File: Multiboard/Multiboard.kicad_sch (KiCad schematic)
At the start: 0 parts

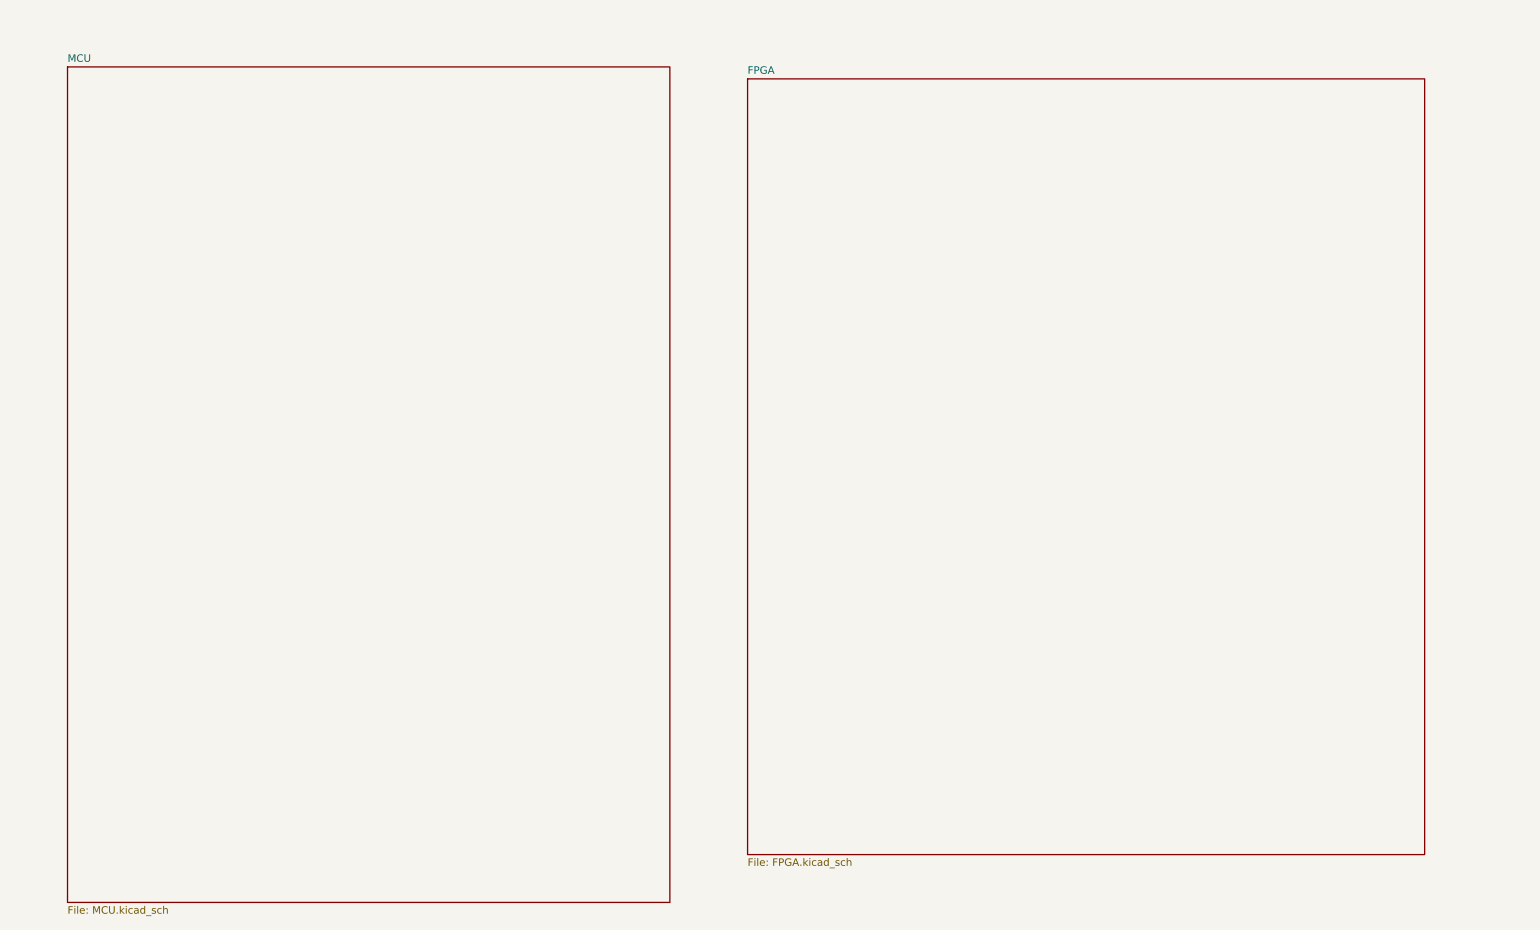
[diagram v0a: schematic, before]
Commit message: completed v1 FPGA schematic
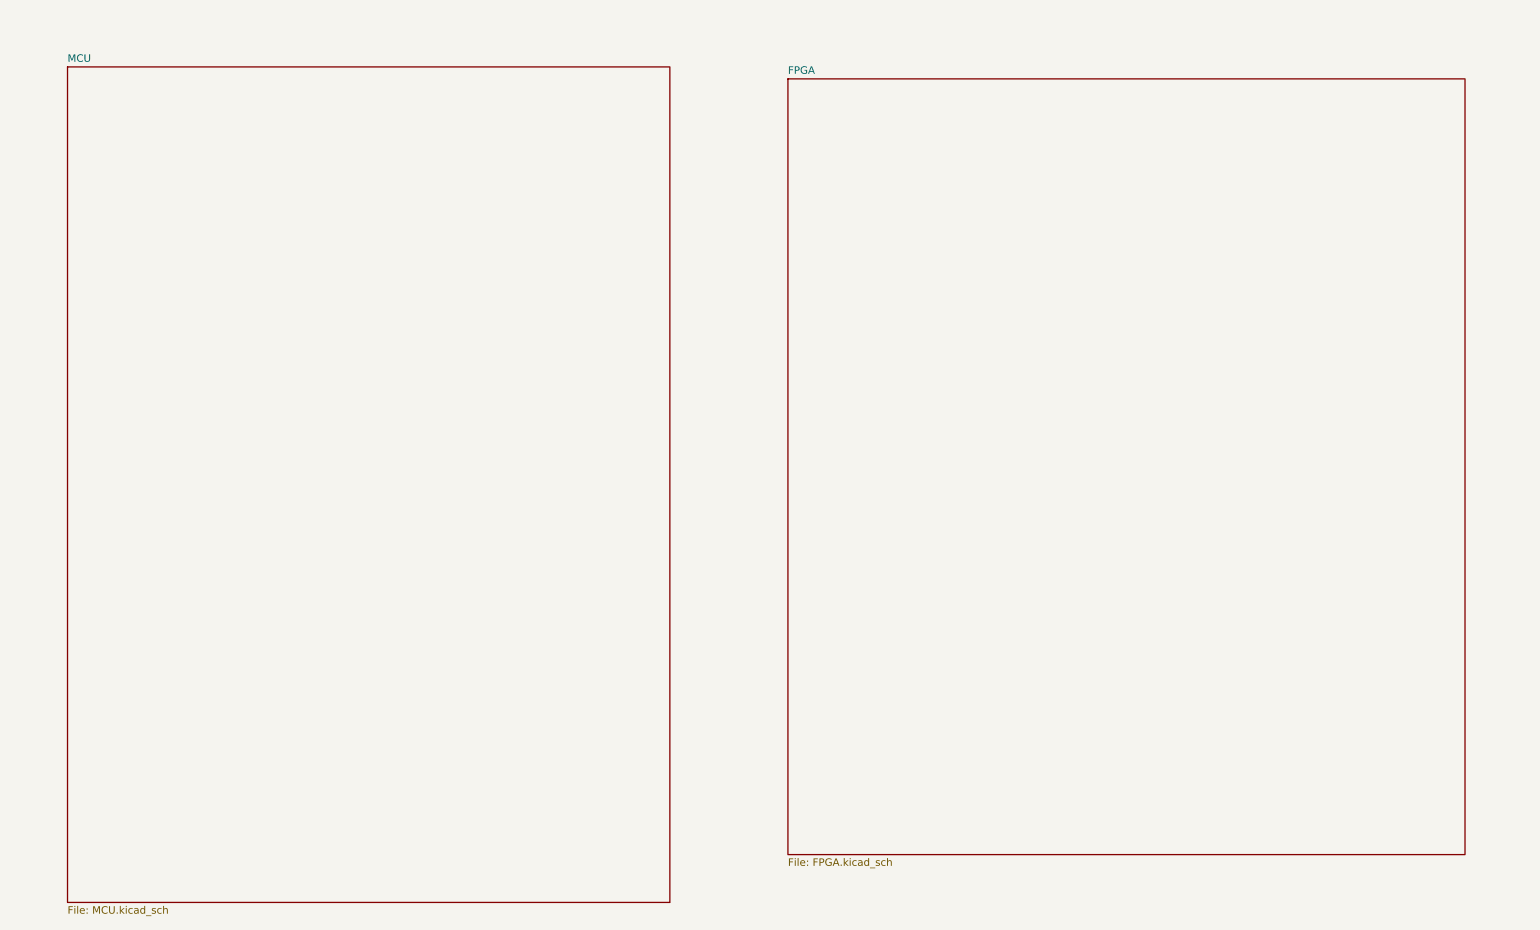
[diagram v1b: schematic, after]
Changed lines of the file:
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@@
 	)
 	(sheet
-		(at 140.716 26.67)
+		(at 147.574 26.67)
 		(size 115.062 131.826)
 		(exclude_from_sim no)
@@
 		)
 		(property "Sheetname" "FPGA"
-			(at 140.716 25.9584 0)
+			(at 147.574 25.9584 0)
 			(effects
 				(font
@@
 		)
 		(property "Sheetfile" "FPGA.kicad_sch"
-			(at 140.716 159.0806 0)
+			(at 147.574 159.0806 0)
 			(effects
 				(font

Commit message: fixed fpga header issue
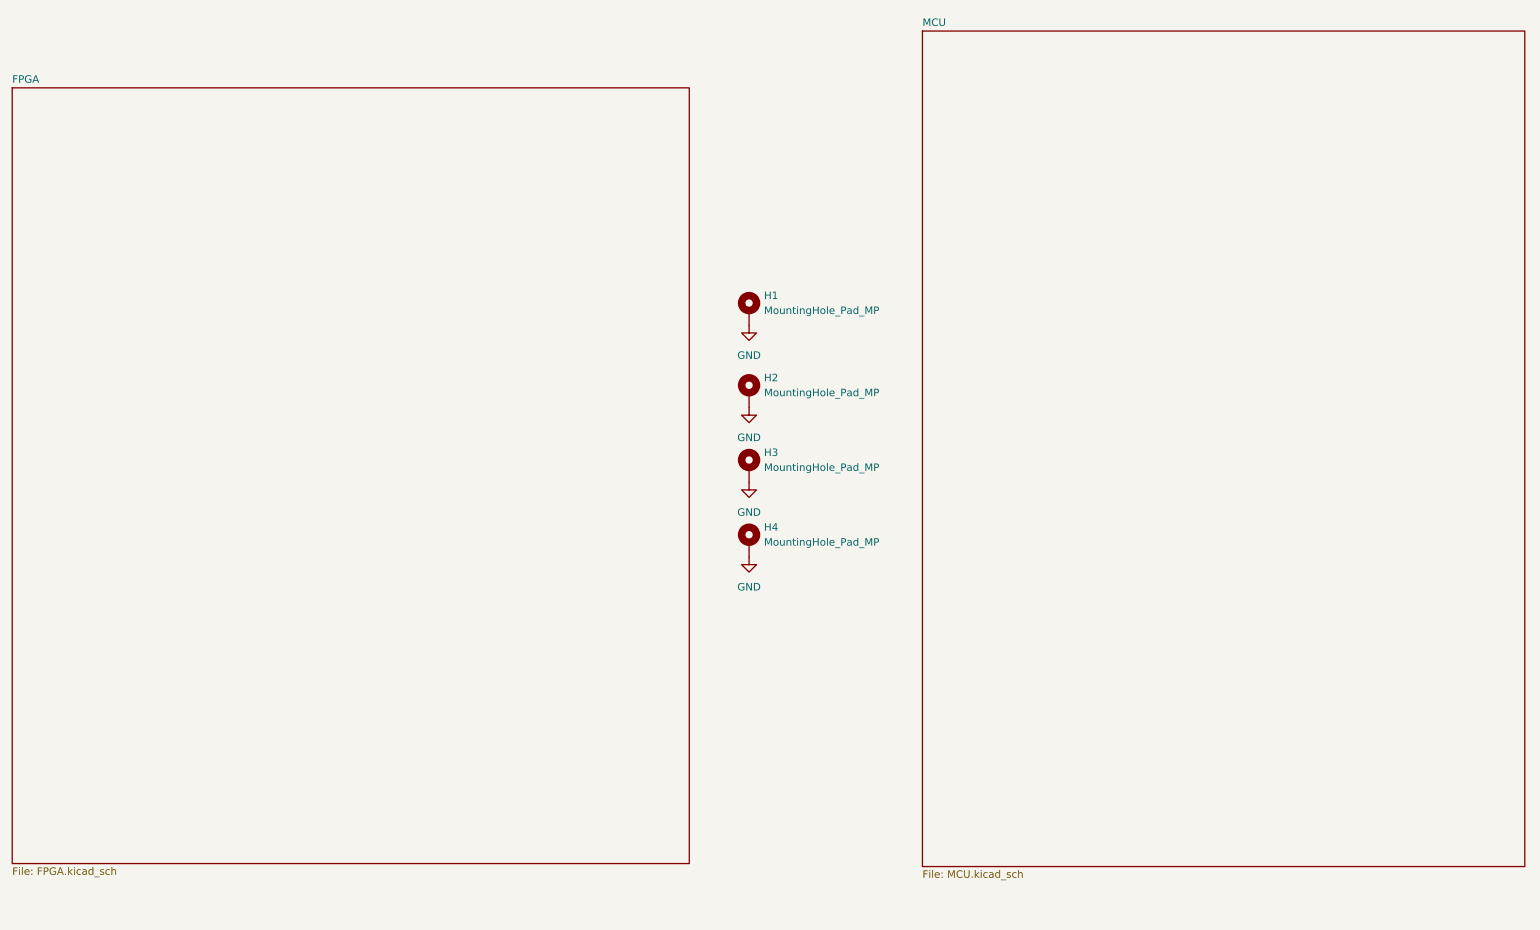
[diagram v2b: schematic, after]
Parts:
- added H1, H2, H3, H4: MountingHole_Pad_MP, MountingHole:MountingHole_3.2mm_M3_DIN965_Pad_TopBottom, symbol Mechanical:MountingHole_Pad_MP
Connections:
- new net GND: H1.MP, H2.MP, H3.MP, H4.MP

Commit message: added elsys logo and project name to silkscreen
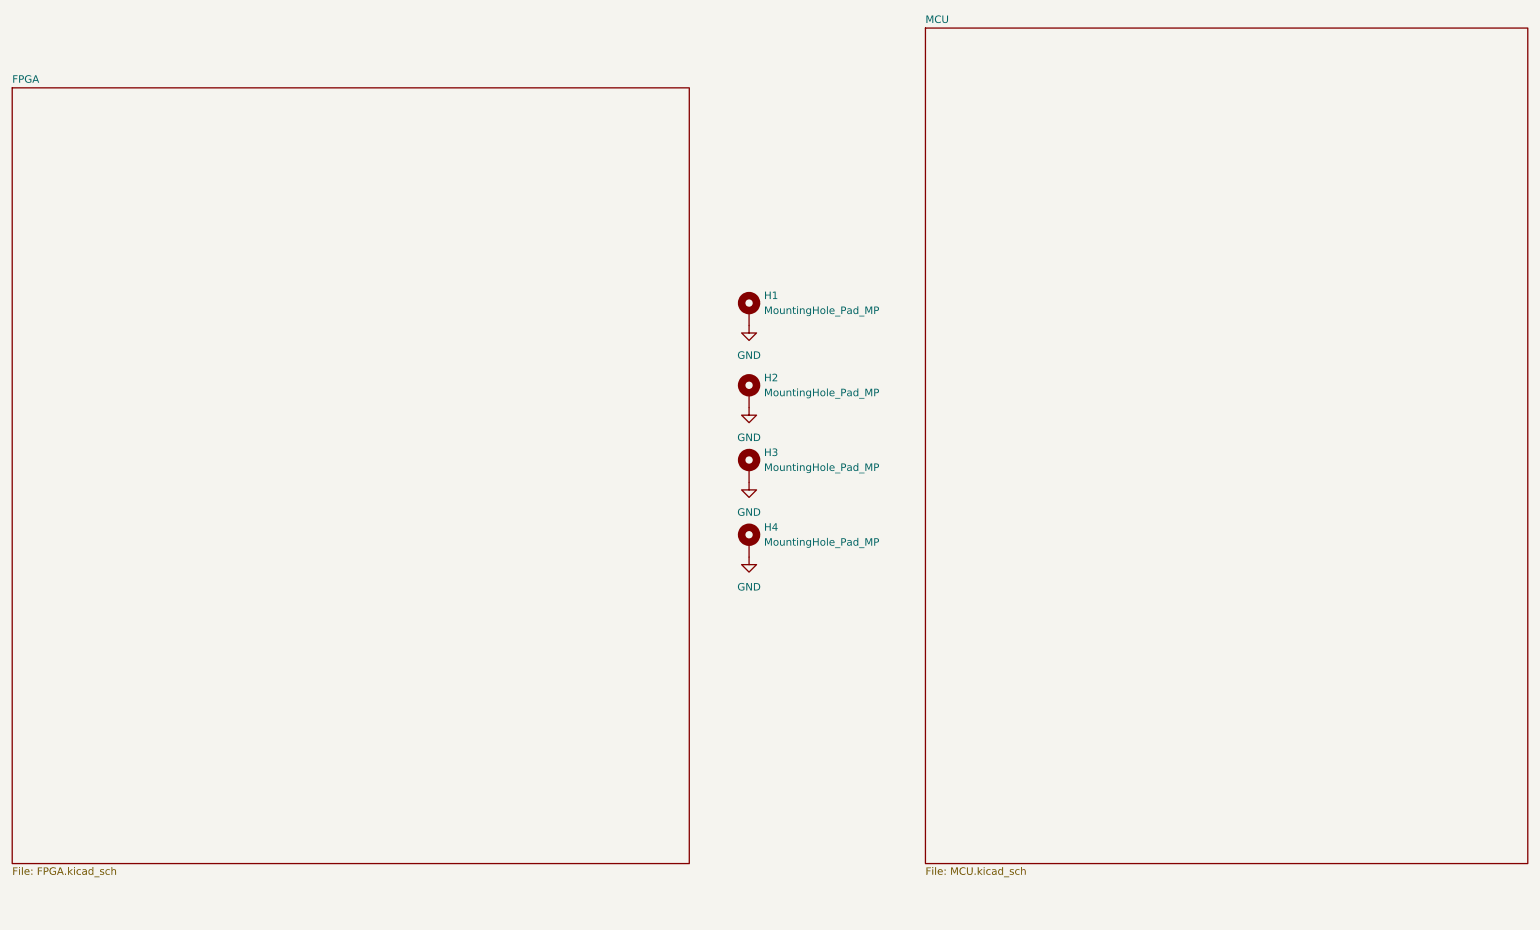
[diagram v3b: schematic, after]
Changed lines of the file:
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@@
 	)
 	(sheet
-		(at 170.434 18.542)
+		(at 170.942 18.034)
 		(size 102.362 141.986)
 		(exclude_from_sim no)
@@
 		)
 		(property "Sheetname" "MCU"
-			(at 170.434 17.8304 0)
+			(at 170.942 17.3224 0)
 			(effects
 				(font
@@
 		)
 		(property "Sheetfile" "MCU.kicad_sch"
-			(at 170.434 161.1126 0)
+			(at 170.942 160.6046 0)
 			(effects
 				(font

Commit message: cleared part of errors and warnings
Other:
- company: (none) -> Technological School "Electronic Systems"
- title: (none) -> IR-Multiboard
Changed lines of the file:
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@@
 	(generator_version "9.0")
 	(paper "A4")
+	(title_block
+		(title "IR-Multiboard")
+		(date "2026-02-23")
+		(company "Technological School \"Electronic Systems\"")
+	)
 	(symbol
 		(lib_id "Mechanical:MountingHole_Pad_MP")

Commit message: Generated BOM
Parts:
- H1, H2, H3, H4: now in the parts list
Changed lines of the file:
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@@
 		(unit 1)
 		(exclude_from_sim no)
-		(in_bom no)
-		(on_board yes)
+		(in_bom yes)
+		(on_board no)
 		(dnp no)
 		(fields_autoplaced yes)
@@
 			)
 		)
+		(property "LCSC Part Number" ""
+			(at 140.97 92.71 0)
+			(effects
+				(font
+					(size 1.27 1.27)
+				)
+				(hide yes)
+			)
+		)
 		(pin "MP"
 		)
@@
 		(unit 1)
 		(exclude_from_sim no)
-		(in_bom no)
-		(on_board yes)
+		(in_bom yes)
+		(on_board no)
 		(dnp no)
 		(fields_autoplaced yes)
@@
 			)
 		)
+		(property "LCSC Part Number" ""
+			(at 140.97 66.04 0)
+			(effects
+				(font
+					(size 1.27 1.27)
+				)
+				(hide yes)
+			)
+		)
 		(pin "MP"
 		)
@@
 		(unit 1)
 		(exclude_from_sim no)
-		(in_bom no)
-		(on_board yes)
+		(in_bom yes)
+		(on_board no)
 		(dnp no)
 		(fields_autoplaced yes)
@@
 			)
 		)
+		(property "LCSC Part Number" ""
+			(at 140.97 80.01 0)
+			(effects
+				(font
+					(size 1.27 1.27)
+				)
+				(hide yes)
+			)
+		)
 		(pin "MP"
 		)
@@
 		(unit 1)
 		(exclude_from_sim no)
-		(in_bom no)
-		(on_board yes)
+		(in_bom yes)
+		(on_board no)
 		(dnp no)
 		(fields_autoplaced yes)
@@
 			(at 140.97 105.41 0)
 			(effects
+				(font
+					(size 1.27 1.27)
+				)
+				(hide yes)
+			)
+		)
+		(property "LCSC Part Number" ""
+			(at 140.97 105.41 0)
+			(effects

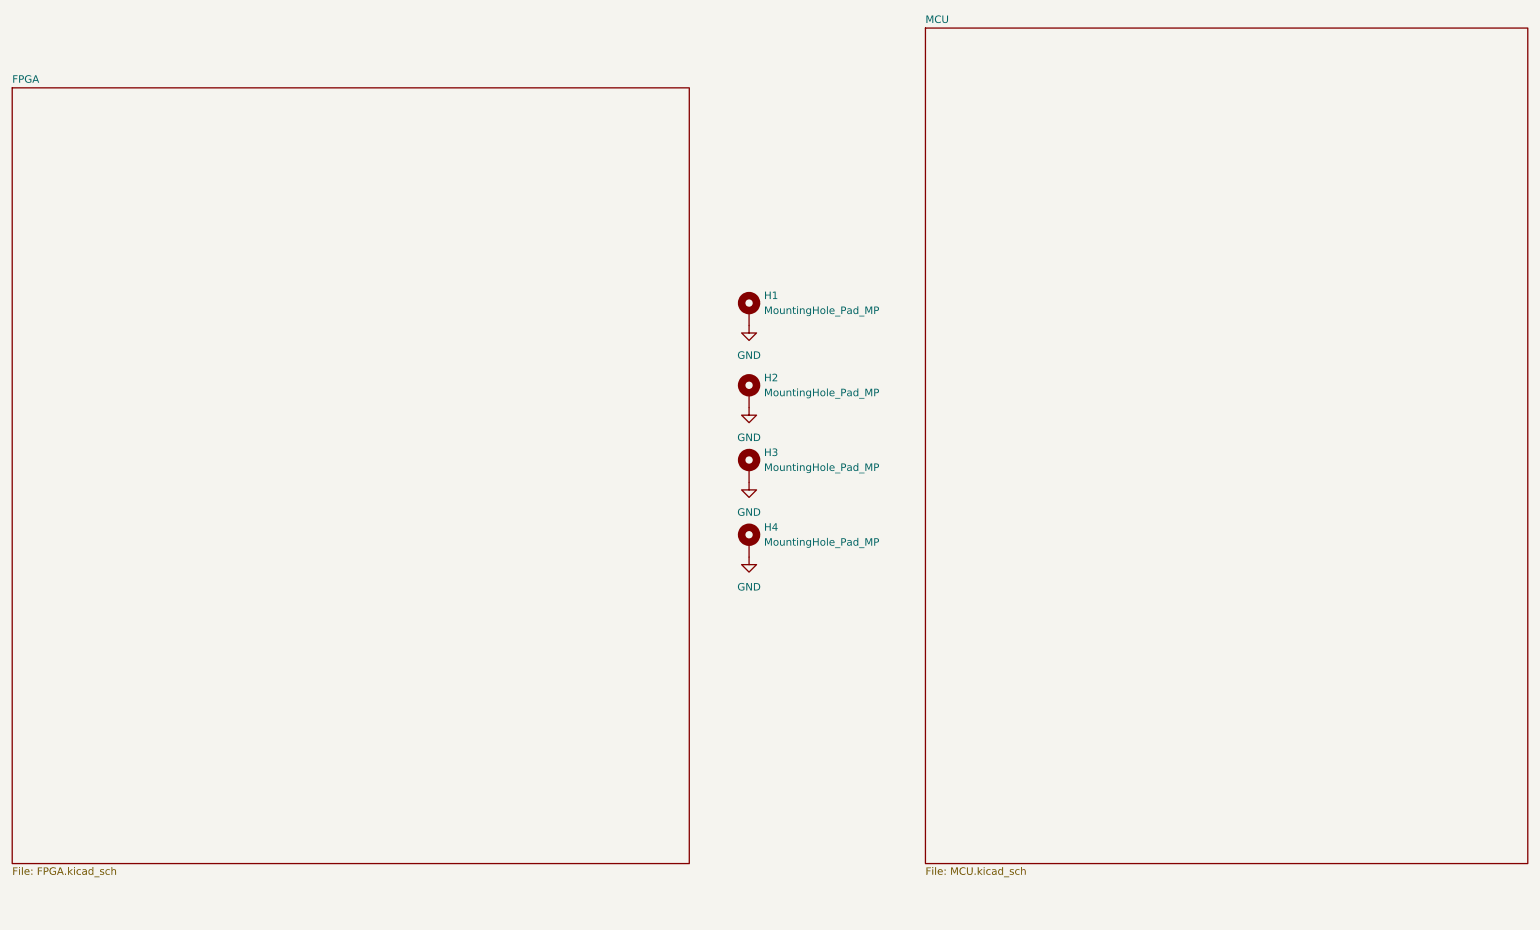
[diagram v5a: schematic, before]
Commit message: Fixed glitched nets issue
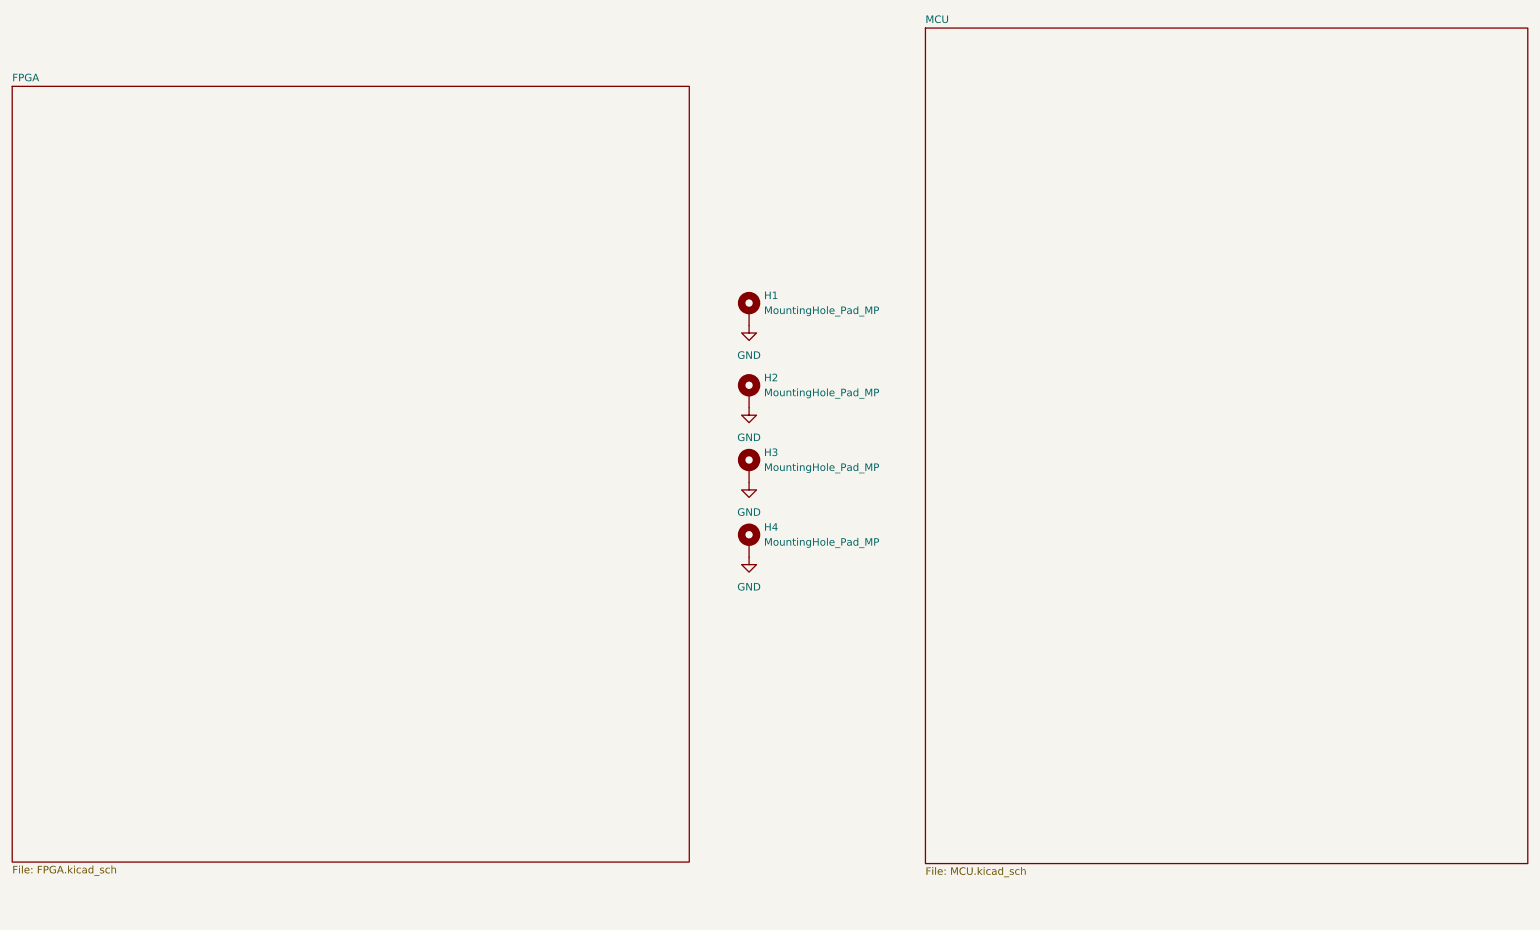
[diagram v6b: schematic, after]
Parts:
- H1, H2, H3, H4: now left out of the parts list
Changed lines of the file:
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@@
 		(unit 1)
 		(exclude_from_sim no)
-		(in_bom yes)
-		(on_board no)
+		(in_bom no)
+		(on_board yes)
 		(dnp no)
 		(fields_autoplaced yes)
@@
 		(unit 1)
 		(exclude_from_sim no)
-		(in_bom yes)
-		(on_board no)
+		(in_bom no)
+		(on_board yes)
 		(dnp no)
 		(fields_autoplaced yes)
@@
 		(unit 1)
 		(exclude_from_sim no)
-		(in_bom yes)
-		(on_board no)
+		(in_bom no)
+		(on_board yes)
 		(dnp no)
 		(fields_autoplaced yes)
@@
 		(unit 1)
 		(exclude_from_sim no)
-		(in_bom yes)
-		(on_board no)
+		(in_bom no)
+		(on_board yes)
 		(dnp no)
 		(fields_autoplaced yes)
@@
 	)
 	(sheet
-		(at 15.748 28.194)
+		(at 15.748 27.94)
 		(size 115.062 131.826)
 		(exclude_from_sim no)
@@
 		)
 		(property "Sheetname" "FPGA"
-			(at 15.748 27.4824 0)
+			(at 15.748 27.2284 0)
 			(effects
 				(font
@@
 		)
 		(property "Sheetfile" "FPGA.kicad_sch"
-			(at 15.748 160.6046 0)
-			(effects
-				(font
+			(at 15.748 160.3506 0)
+			(effects
+				(font
